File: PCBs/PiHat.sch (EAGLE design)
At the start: 19 parts, among them U1 TLV70036DDCTDDC5-L

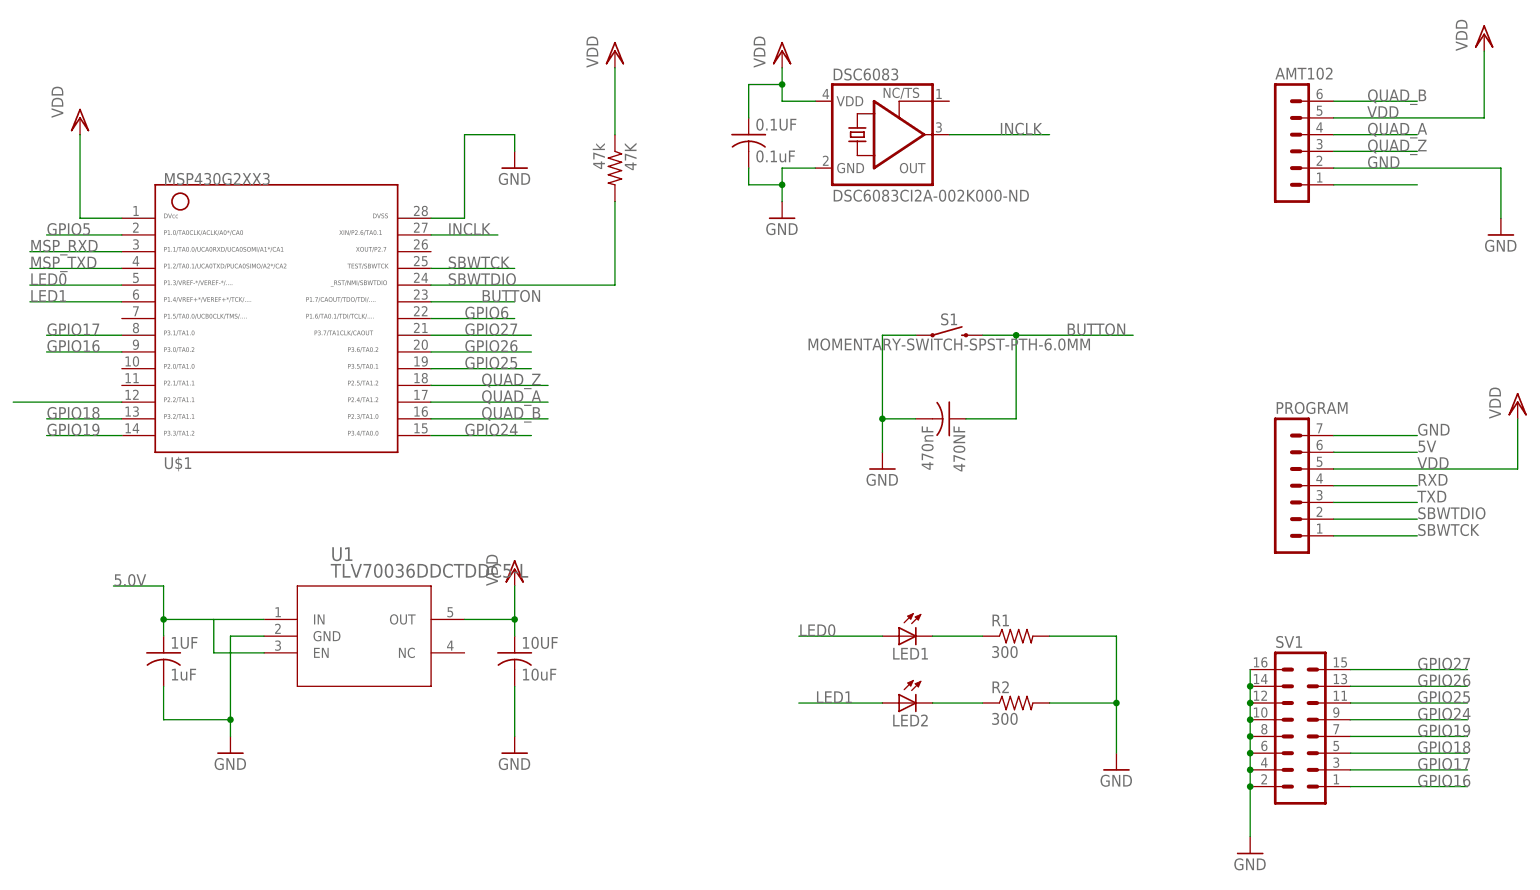
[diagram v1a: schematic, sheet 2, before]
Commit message: Updated code some more trying to get 2kHz clock to work
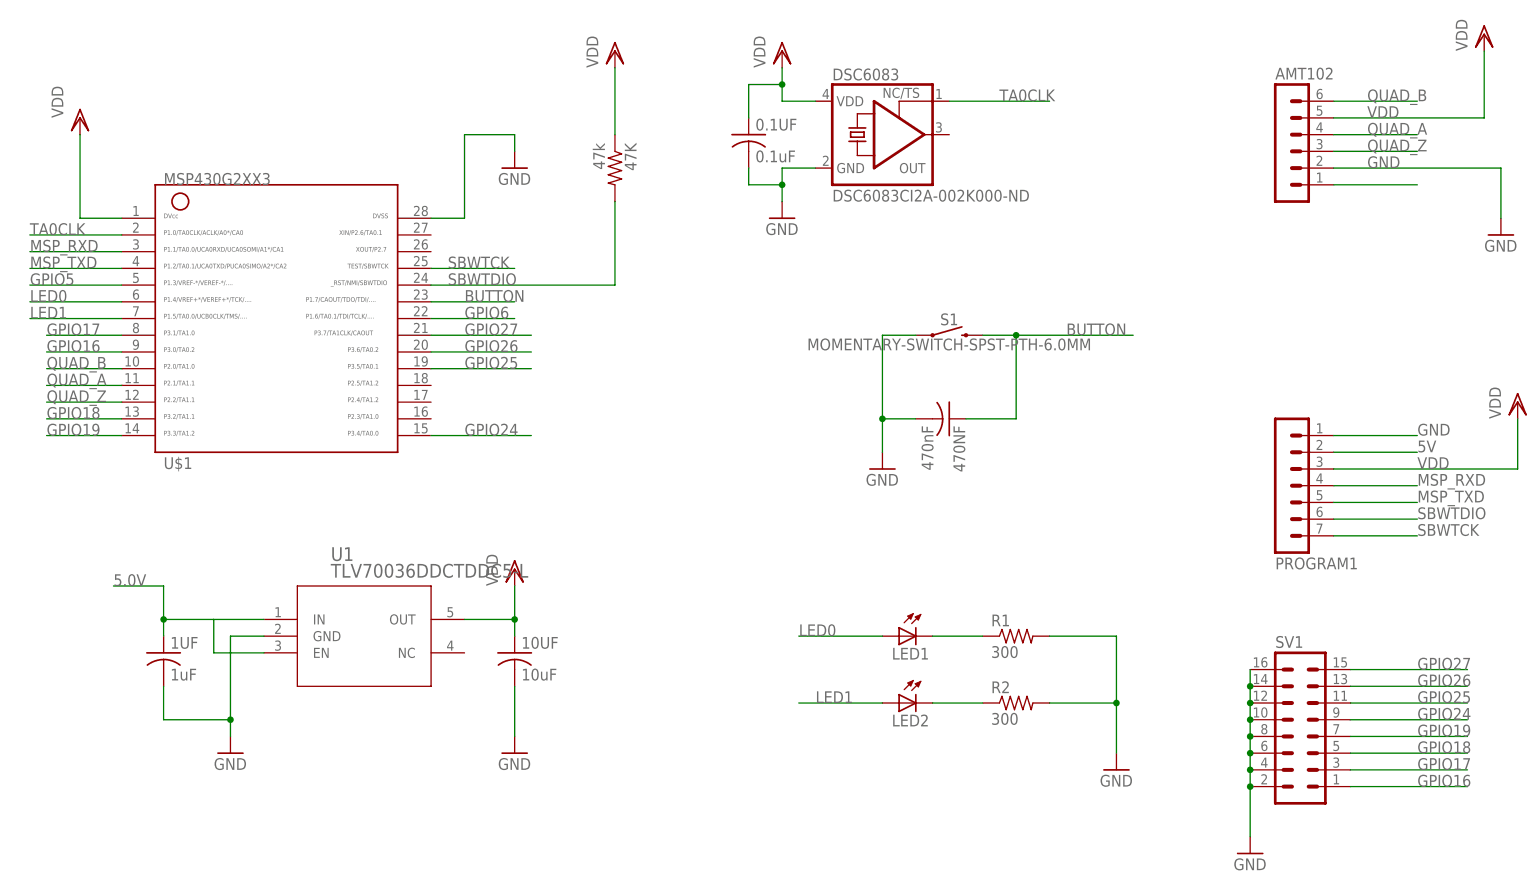
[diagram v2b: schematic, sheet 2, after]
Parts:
- renumbered PROGRAM to PROGRAM1
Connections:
- removed net INCLK: DSC6083.OUT, U$1.27
- removed net N$4: U$1.12
- removed net RXD: PROGRAM1.4
- removed net TXD: PROGRAM1.3
- new net TA0CLK: DSC6083.TS, U$1.2
- net 5V: now also PROGRAM1.2; no longer PROGRAM1.6
- net GND: now also PROGRAM1.1; no longer PROGRAM1.7
- net GPIO5: now also U$1.5; no longer U$1.2
- net LED0: now also U$1.6; no longer U$1.5
- net LED1: now also U$1.7; no longer U$1.6
- net MSP_RXD: now also PROGRAM1.4
- net MSP_TXD: now also PROGRAM1.5
- net QUAD_A: now also U$1.11; no longer U$1.17
- net QUAD_B: now also U$1.10; no longer U$1.16
- net QUAD_Z: now also U$1.12; no longer U$1.18
- net SBWTCK: now also PROGRAM1.7; no longer PROGRAM1.1
- net SBWTDIO: now also PROGRAM1.6; no longer PROGRAM1.2
- net VDD: now also PROGRAM1.3; no longer PROGRAM1.5
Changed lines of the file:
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@@
 <?xml version="1.0" encoding="utf-8"?>
 <!DOCTYPE eagle SYSTEM "eagle.dtd">
-<eagle version="9.2.2">
+<eagle version="9.3.2">
 <drawing>
 <settings>
@@
 <part name="SV1" library="con-lstb-mod" deviceset="MA08-2" device="" package3d_urn="urn:adsk.eagle:package:8335/1"/>
 <part name="GND7" library="supply1" library_urn="urn:adsk.eagle:library:371" deviceset="GND" device=""/>
-<part name="PROGRAM" library="con-lstb-mod" deviceset="MA07-1" device="" package3d_urn="urn:adsk.eagle:package:8341/1"/>
 <part name="AMT102" library="con-lstb-mod" deviceset="MA06-1" device="" package3d_urn="urn:adsk.eagle:package:8340/1"/>
 <part name="U1" library="TLV70036" deviceset="TLV70036DDCT" device="DDC5-L"/>
+<part name="PROGRAM1" library="con-lstb-mod" deviceset="MA07-1" device="" package3d_urn="urn:adsk.eagle:package:8341/1"/>
 </parts>
 <sheets>
@@
 <attribute name="VALUE" x="81.28" y="-60.96" size="1.778" layer="96"/>
 </instance>
-<instance part="PROGRAM" gate="1" x="88.9" y="-2.54" smashed="yes">
-<attribute name="VALUE" x="87.63" y="-15.24" size="1.778" layer="96"/>
-<attribute name="NAME" x="87.63" y="8.382" size="1.778" layer="95"/>
-</instance>
 <instance part="AMT102" gate="1" x="88.9" y="50.8" smashed="yes">
 <attribute name="VALUE" x="87.63" y="38.1" size="1.778" layer="96"/>
@@
 <attribute name="NAME" x="-55.88" y="-13.97" size="2.0828" layer="95" ratio="6" rot="SR0"/>
 <attribute name="VALUE" x="-55.88" y="-16.51" size="2.0828" layer="96" ratio="6" rot="SR0"/>
+</instance>
+<instance part="PROGRAM1" gate="1" x="88.9" y="-2.54" smashed="yes" rot="MR180">
+<attribute name="VALUE" x="87.63" y="10.16" size="1.778" layer="96" rot="MR180"/>
+<attribute name="NAME" x="87.63" y="-13.462" size="1.778" layer="95" rot="MR180"/>
 </instance>
 </instances>
@@
 <wire x1="124.46" y1="0" x2="124.46" y2="7.62" width="0.1524" layer="91"/>
 <pinref part="VDD1" gate="G$1" pin="VDD"/>
-<pinref part="PROGRAM" gate="1" pin="5"/>
+<pinref part="PROGRAM1" gate="1" pin="3"/>
 </segment>
 <segment>
@@
 <wire x1="96.52" y1="5.08" x2="109.22" y2="5.08" width="0.1524" layer="91"/>
 <label x="109.22" y="5.08" size="1.778" layer="95"/>
-<pinref part="PROGRAM" gate="1" pin="7"/>
+<pinref part="PROGRAM1" gate="1" pin="1"/>
 </segment>
 <segment>
@@
 <pinref part="U$1" gate="G$1" pin="23"/>
 <wire x1="-40.64" y1="25.4" x2="-27.94" y2="25.4" width="0.1524" layer="91"/>
-<label x="-33.02" y="25.4" size="1.778" layer="95"/>
+<label x="-35.56" y="25.4" size="1.778" layer="95"/>
 </segment>
 </net>
@@
 <wire x1="96.52" y1="2.54" x2="109.22" y2="2.54" width="0.1524" layer="91"/>
 <label x="109.22" y="2.54" size="1.778" layer="95"/>
-<pinref part="PROGRAM" gate="1" pin="6"/>
-</segment>
-</net>
-<net name="TXD" class="0">
-<segment>
-<wire x1="96.52" y1="-5.08" x2="109.22" y2="-5.08" width="0.1524" layer="91"/>
-<label x="109.22" y="-5.08" size="1.778" layer="95"/>
-<pinref part="PROGRAM" gate="1" pin="3"/>
+<pinref part="PROGRAM1" gate="1" pin="2"/>
 </segment>
 </net>
@@
 <wire x1="96.52" y1="-7.62" x2="109.22" y2="-7.62" width="0.1524" layer="91"/>
 <label x="109.22" y="-7.62" size="1.778" layer="95"/>
-<pinref part="PROGRAM" gate="1" pin="2"/>
+<pinref part="PROGRAM1" gate="1" pin="6"/>
 </segment>
 <segment>
@@
 <wire x1="96.52" y1="-10.16" x2="109.22" y2="-10.16" width="0.1524" layer="91"/>
 <label x="109.22" y="-10.16" size="1.778" layer="95"/>
-<pinref part="PROGRAM" gate="1" pin="1"/>
+<pinref part="PROGRAM1" gate="1" pin="7"/>
 </segment>
 <segment>
@@
 </segment>
 </net>
-<net name="RXD" class="0">
-<segment>
-<wire x1="96.52" y1="-2.54" x2="109.22" y2="-2.54" width="0.1524" layer="91"/>
-<label x="109.22" y="-2.54" size="1.778" layer="95"/>
-<pinref part="PROGRAM" gate="1" pin="4"/>
-</segment>
-</net>
 <net name="GPIO17" class="0">
 <segment>
@@
 </segment>
 <segment>
-<pinref part="U$1" gate="G$1" pin="18"/>
-<wire x1="-40.64" y1="12.7" x2="-22.86" y2="12.7" width="0.1524" layer="91"/>
-<label x="-33.02" y="12.7" size="1.778" layer="95"/>
+<pinref part="U$1" gate="G$1" pin="12"/>
+<wire x1="-87.63" y1="10.16" x2="-99.06" y2="10.16" width="0.1524" layer="91"/>
+<label x="-99.06" y="10.16" size="1.778" layer="95"/>
 </segment>
 </net>
@@
 </segment>
 <segment>
-<pinref part="U$1" gate="G$1" pin="16"/>
-<wire x1="-40.64" y1="7.62" x2="-22.86" y2="7.62" width="0.1524" layer="91"/>
-<label x="-33.02" y="7.62" size="1.778" layer="95"/>
+<pinref part="U$1" gate="G$1" pin="10"/>
+<wire x1="-87.63" y1="15.24" x2="-99.06" y2="15.24" width="0.1524" layer="91"/>
+<label x="-99.06" y="15.24" size="1.778" layer="95"/>
 </segment>
 </net>
@@
 </segment>
 <segment>
-<pinref part="U$1" gate="G$1" pin="17"/>
-<wire x1="-40.64" y1="10.16" x2="-22.86" y2="10.16" width="0.1524" layer="91"/>
-<label x="-33.02" y="10.16" size="1.778" layer="95"/>
+<pinref part="U$1" gate="G$1" pin="11"/>
+<wire x1="-87.63" y1="12.7" x2="-99.06" y2="12.7" width="0.1524" layer="91"/>
+<label x="-99.06" y="12.7" size="1.778" layer="95"/>
 </segment>
 </net>
@@
 <label x="-101.6" y="30.48" size="1.778" layer="95"/>
 </segment>
+<segment>
+<wire x1="96.52" y1="-5.08" x2="109.22" y2="-5.08" width="0.1524" layer="91"/>
+<label x="109.22" y="-5.08" size="1.778" layer="95"/>
+<pinref part="PROGRAM1" gate="1" pin="5"/>
+</segment>
 </net>
 <net name="MSP_RXD" class="0">
@@
 <wire x1="-87.63" y1="33.02" x2="-101.6" y2="33.02" width="0.1524" layer="91"/>
 <label x="-101.6" y="33.02" size="1.778" layer="95"/>
+</segment>
+<segment>
+<wire x1="96.52" y1="-2.54" x2="109.22" y2="-2.54" width="0.1524" layer="91"/>
+<label x="109.22" y="-2.54" size="1.778" layer="95"/>
+<pinref part="PROGRAM1" gate="1" pin="4"/>
 </segment>
 </net>
@@
 </segment>
 </net>
-<net name="INCLK" class="0">
-<segment>
-<pinref part="DSC6083" gate="G$1" pin="OUT"/>
-<wire x1="38.1" y1="50.8" x2="53.34" y2="50.8" width="0.1524" layer="91"/>
-<label x="45.72" y="50.8" size="1.778" layer="95"/>
-</segment>
-<segment>
-<pinref part="U$1" gate="G$1" pin="27"/>
-<wire x1="-40.64" y1="35.56" x2="-30.48" y2="35.56" width="0.1524" layer="91"/>
-<label x="-38.1" y="35.56" size="1.778" layer="95"/>
-</segment>
-</net>
 <net name="LED1" class="0">
 <segment>
@@
 </segment>
 <segment>
+<pinref part="U$1" gate="G$1" pin="7"/>
+<wire x1="-87.63" y1="22.86" x2="-101.6" y2="22.86" width="0.1524" layer="91"/>
+<label x="-101.6" y="22.86" size="1.778" layer="95"/>
+</segment>
+</net>
+<net name="GPIO6" class="0">
+<segment>
+<pinref part="U$1" gate="G$1" pin="22"/>
+<wire x1="-40.64" y1="22.86" x2="-27.94" y2="22.86" width="0.1524" layer="91"/>
+<label x="-35.56" y="22.86" size="1.778" layer="95"/>
+</segment>
+</net>
+<net name="LED0" class="0">
+<segment>
+<pinref part="LED1" gate="G$1" pin="A"/>
+<wire x1="27.94" y1="-25.4" x2="15.24" y2="-25.4" width="0.1524" layer="91"/>
+<label x="15.24" y="-25.4" size="1.778" layer="95"/>
+</segment>
+<segment>
 <pinref part="U$1" gate="G$1" pin="6"/>
 <wire x1="-87.63" y1="25.4" x2="-101.6" y2="25.4" width="0.1524" layer="91"/>
@@
 </segment>
 </net>
+<net name="N$1" class="0">
+<segment>
+<pinref part="LED1" gate="G$1" pin="C"/>
+<pinref part="R1" gate="G$1" pin="1"/>
+<wire x1="43.18" y1="-25.4" x2="35.56" y2="-25.4" width="0.1524" layer="91"/>
+</segment>
+</net>
+<net name="N$2" class="0">
+<segment>
+<pinref part="LED2" gate="G$1" pin="C"/>
+<pinref part="R2" gate="G$1" pin="1"/>
+<wire x1="43.18" y1="-35.56" x2="35.56" y2="-35.56" width="0.1524" layer="91"/>
+</segment>
+</net>
+<net name="TA0CLK" class="0">
+<segment>
+<pinref part="U$1" gate="G$1" pin="2"/>
+<wire x1="-87.63" y1="35.56" x2="-101.6" y2="35.56" width="0.1524" layer="91"/>
+<label x="-101.6" y="35.56" size="1.778" layer="95"/>
+</segment>
+<segment>
+<pinref part="DSC6083" gate="G$1" pin="TS"/>
+<wire x1="38.1" y1="55.88" x2="53.34" y2="55.88" width="0.1524" layer="91"/>
+<label x="45.72" y="55.88" size="1.778" layer="95"/>
+</segment>
+</net>
 <net name="GPIO5" class="0">
-<segment>
-<pinref part="U$1" gate="G$1" pin="2"/>
-<wire x1="-87.63" y1="35.56" x2="-99.06" y2="35.56" width="0.1524" layer="91"/>
-<label x="-99.06" y="35.56" size="1.778" layer="95"/>
-</segment>
-</net>
-<net name="GPIO6" class="0">
-<segment>
-<pinref part="U$1" gate="G$1" pin="22"/>
-<wire x1="-40.64" y1="22.86" x2="-27.94" y2="22.86" width="0.1524" layer="91"/>
-<label x="-35.56" y="22.86" size="1.778" layer="95"/>
-</segment>
-</net>
-<net name="LED0" class="0">
-<segment>
-<pinref part="LED1" gate="G$1" pin="A"/>
-<wire x1="27.94" y1="-25.4" x2="15.24" y2="-25.4" width="0.1524" layer="91"/>
-<label x="15.24" y="-25.4" size="1.778" layer="95"/>
-</segment>
 <segment>
 <pinref part="U$1" gate="G$1" pin="5"/>
@@
 </segment>
 </net>
-<net name="N$1" class="0">
-<segment>
-<pinref part="LED1" gate="G$1" pin="C"/>
-<pinref part="R1" gate="G$1" pin="1"/>
-<wire x1="43.18" y1="-25.4" x2="35.56" y2="-25.4" width="0.1524" layer="91"/>
-</segment>
-</net>
-<net name="N$2" class="0">
-<segment>
-<pinref part="LED2" gate="G$1" pin="C"/>
-<pinref part="R2" gate="G$1" pin="1"/>
-<wire x1="43.18" y1="-35.56" x2="35.56" y2="-35.56" width="0.1524" layer="91"/>
-</segment>
-</net>
-<net name="N$4" class="0">
-<segment>
-<pinref part="U$1" gate="G$1" pin="12"/>
-<wire x1="-87.63" y1="10.16" x2="-104.14" y2="10.16" width="0.1524" layer="91"/>
-</segment>
-</net>

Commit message: Fixed errors and added a FT230 USB/UART Interface to PCB
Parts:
- added C3: 10nF, resistor:C-USC0603
- added C4: 100nF, resistor:C-USC0603
- added C5, C6: 47pF, resistor:C-USC0603
- added FERRITE: (no value), rcl:R-US_R0805
- added R3, R4: 27R, resistor:R-US_R0603
- added R5, R6: 300, resistor:R-US_R0603
- added RX, TX: (no value), led:LEDCHIPLED_1206
- added U2: FT230, OPL_IC:INTERFACE-FT230XS-R(SSOP16)
- added USB1: MICRO-USB-FCI-10118193, microftx:MICRO-USB-FCI-10118193
- DSC6083: value DSC6083CI2A-002K000-ND -> 2KHZ
- R1, R2: value 300 -> R
- U$1: value G2XX3---PW28 -> MSP430
- renumbered 0.1UF to C, PROGRAM1 to PROGRAM
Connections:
- new net N$10: R5.1, TX.C
- new net N$3: C3.1, FERRITE.1, USB1.V
- new net N$4: C5.1, R3.1, USB1.D-
- new net N$5: R3.2, U2.USBDM
- new net N$7: C6.1, R4.1, USB1.D+
- new net N$8: R4.2, U2.USBDP
- new net N$9: R6.1, RX.C
- new net RXLED: R6.2, U2.CBUS1
- new net TXLED: R5.2, U2.CBUS2
- new net VCCIO: C4.1, RX.A, TX.A, U2.3V3OUT, U2.RESET, U2.VCCIO
- net 5.0V: now also FERRITE.2, U2.VCC
- net GND: now also C3.2, C4.2, C5.2, C6.2, U2.GND, U2.GND@1, USB1.G, USB1.GND1, USB1.GND2, USB1.GND3, USB1.GND4, USB1.GND5, USB1.GND6
- net MSP_RXD: now also U2.TXD
- net MSP_TXD: now also U2.RXD

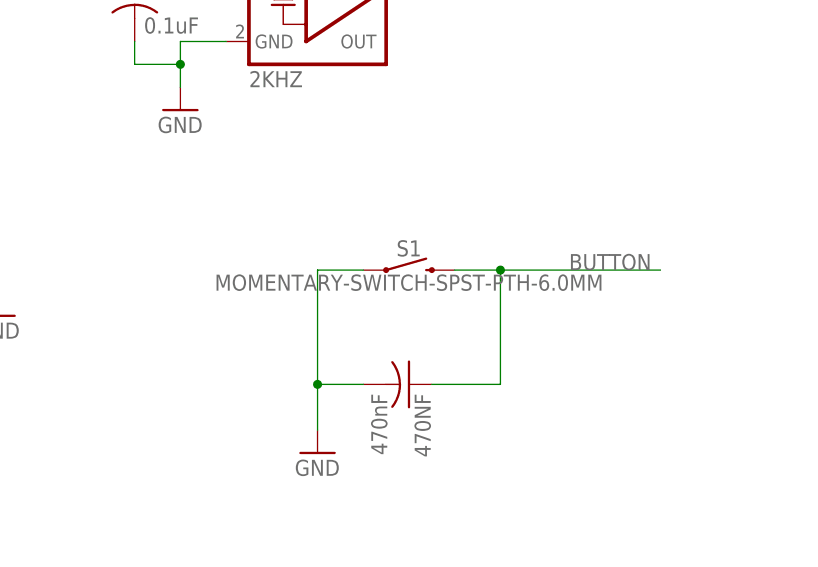
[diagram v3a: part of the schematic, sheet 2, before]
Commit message: Updated interface PCB to have proper silkscreen and added manufacturing files
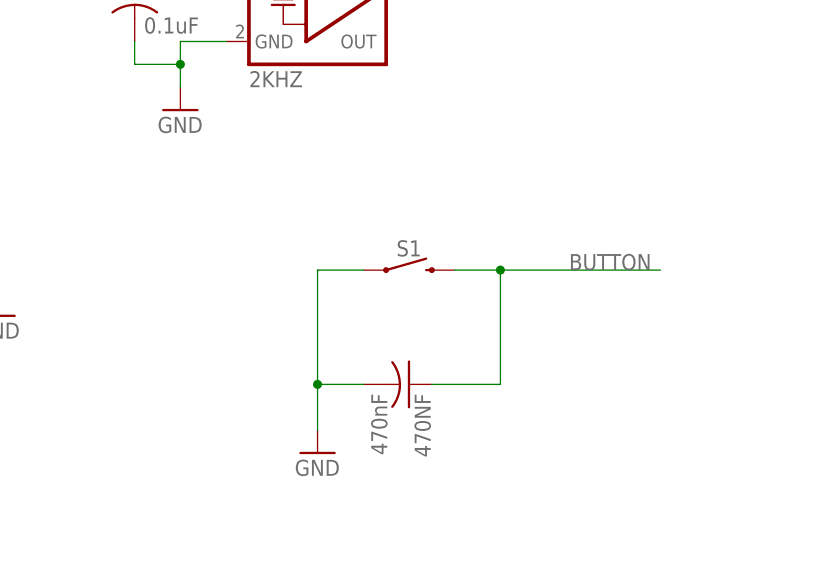
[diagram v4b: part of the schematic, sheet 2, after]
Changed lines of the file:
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@@
 <part name="FID2" library="microbuilder" deviceset="FIDUCIAL" device="&quot;&quot;"/>
 <part name="FID3" library="microbuilder" deviceset="FIDUCIAL" device="&quot;&quot;"/>
-<part name="S1" library="SparkFun-Switches" deviceset="MOMENTARY-SWITCH-SPST" device="-PTH-6.0MM"/>
+<part name="S1" library="SparkFun-Switches" deviceset="MOMENTARY-SWITCH-SPST" device="-PTH-6.0MM" value=""/>
 <part name="GND6" library="supply1" library_urn="urn:adsk.eagle:library:371" deviceset="GND" device=""/>
 <part name="VDD5" library="supply1" library_urn="urn:adsk.eagle:library:371" deviceset="VDD" device=""/>
